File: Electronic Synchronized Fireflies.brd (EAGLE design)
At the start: 37 x 35 mm, 30 parts, among them Q1 BSS123, Q2 BSS84, Q3 LPT80A, Q4 LPT80A, Q5 LPT80A, U1 NCP1400A, U2 MSP430G2231

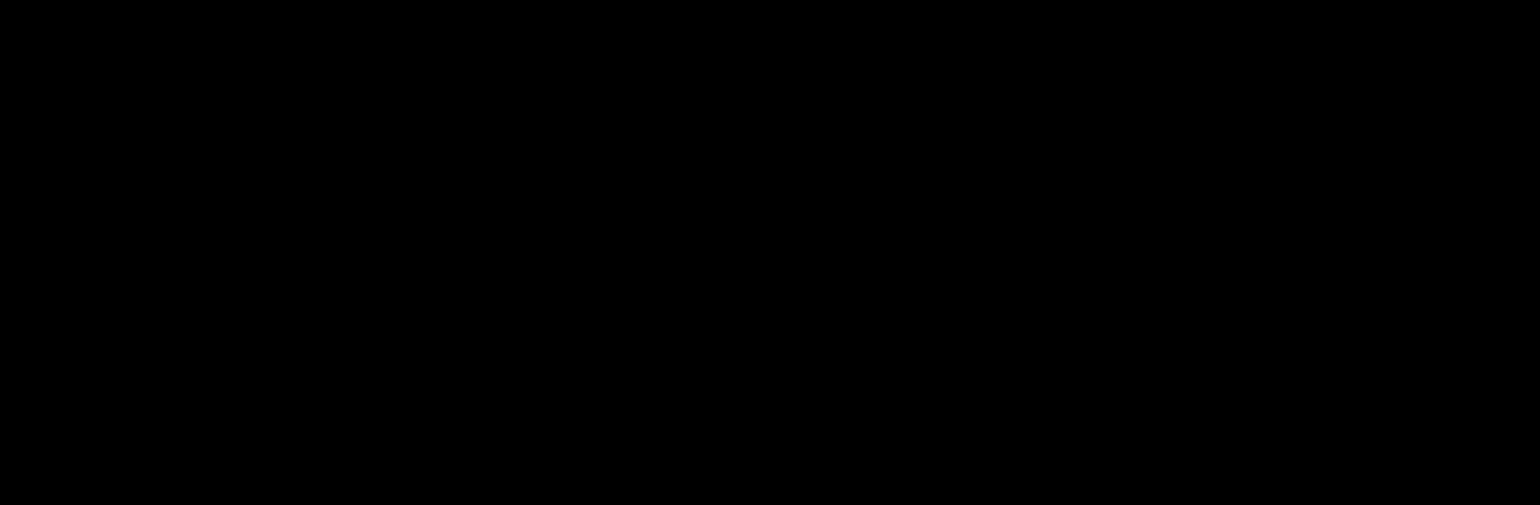
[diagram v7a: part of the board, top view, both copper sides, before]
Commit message: Added detail to document fields (Schematic/PCB)
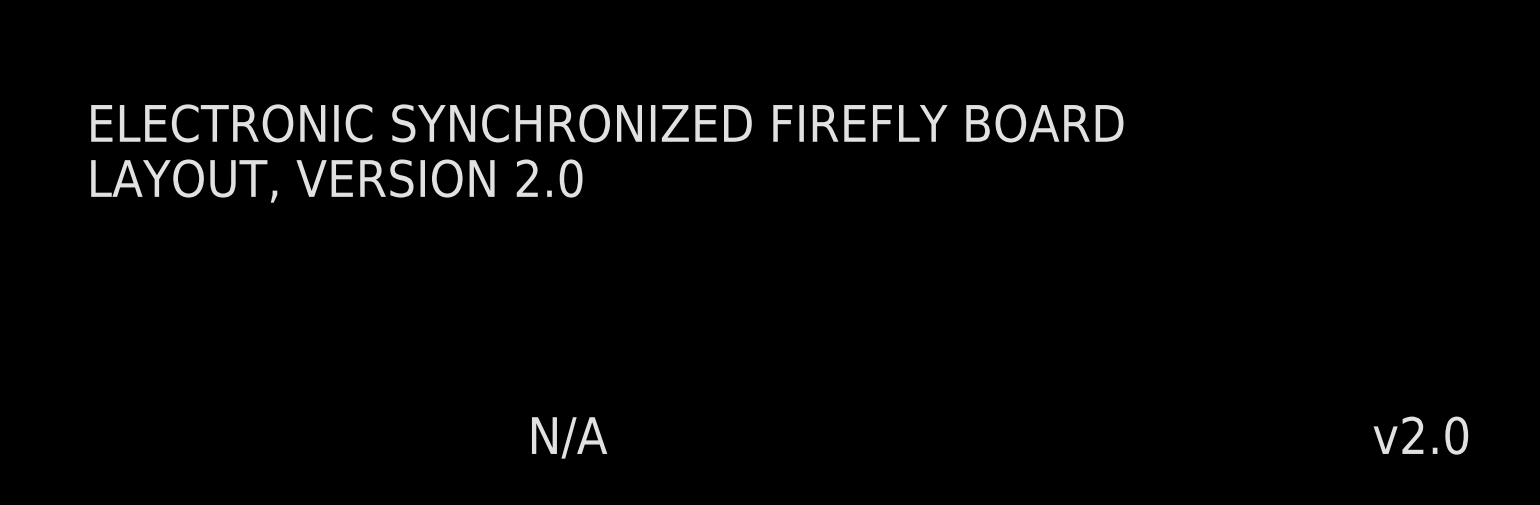
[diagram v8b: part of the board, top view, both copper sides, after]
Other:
- board text added: "ELECTRONIC SYNCHRONIZED FIREFLY BOARD LAYOUT, VERSION 2.0"
- board text added: "N/A"
- board text added: "v2.0"
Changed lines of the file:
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@@
 <setting verticaltext="up"/>
 </settings>
-<grid distance="0.5" unitdist="mm" unit="mm" style="lines" multiple="1" display="yes" altdistance="0.025" altunitdist="inch" altunit="inch"/>
+<grid distance="0.1" unitdist="inch" unit="inch" style="lines" multiple="1" display="yes" altdistance="0.025" altunitdist="inch" altunit="inch"/>
 <layers>
 <layer number="1" name="Top" color="4" fill="1" visible="yes" active="yes"/>
@@
 <hole x="35" y="10" drill="2"/>
 <hole x="18.5" y="33" drill="2"/>
+<text x="91.44" y="-83.82" size="2.54" layer="25">N/A</text>
+<text x="149.86" y="-83.82" size="2.54" layer="25">v2.0</text>
+<text x="60.96" y="-66.04" size="2.54" layer="25">ELECTRONIC SYNCHRONIZED FIREFLY BOARD
+LAYOUT, VERSION 2.0</text>
 </plain>
 <attributes>
@@
 </board>
 </drawing>
+<compatibility>
+<note version="6.3" minversion="6.2.2" severity="warning">
+Since Version 6.2.2 text objects can contain more than one line,
+which will not be processed correctly with this version.
+</note>
+</compatibility>
 </eagle>
